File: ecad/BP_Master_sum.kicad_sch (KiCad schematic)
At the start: 14 parts, among them U11 NE5532, U19 NE5532, U20 PGA231x, U3 NE5532

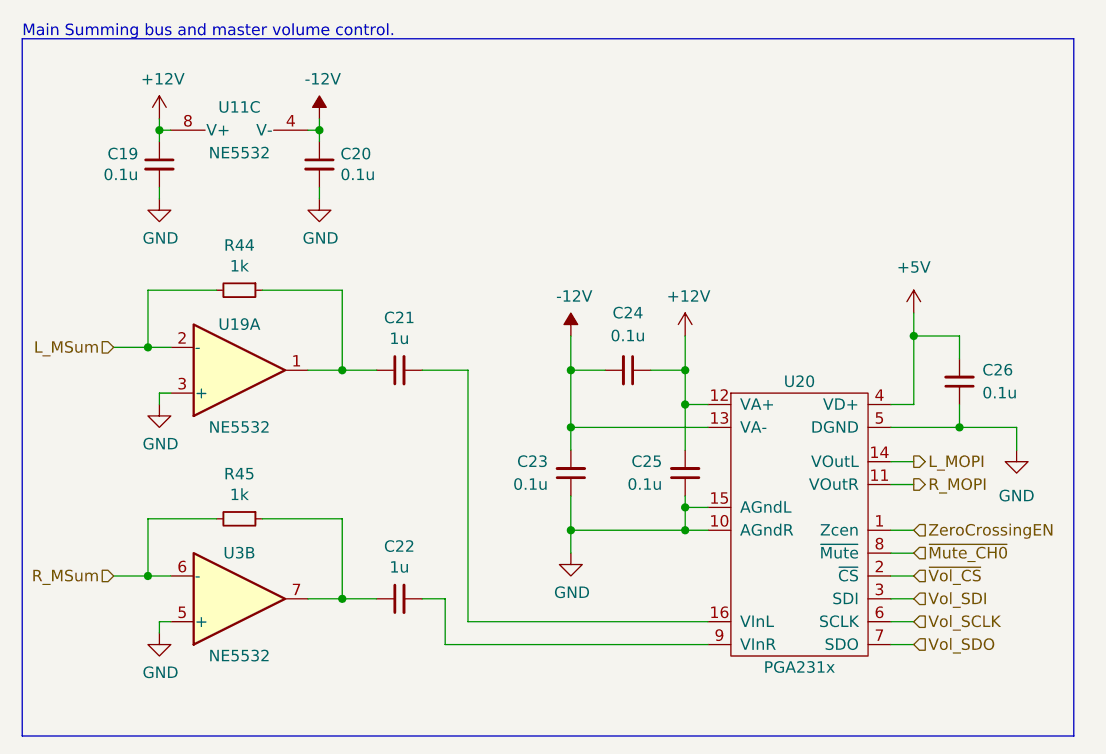
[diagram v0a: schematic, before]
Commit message: Update to Kicad 7 and generate PDF schematic.
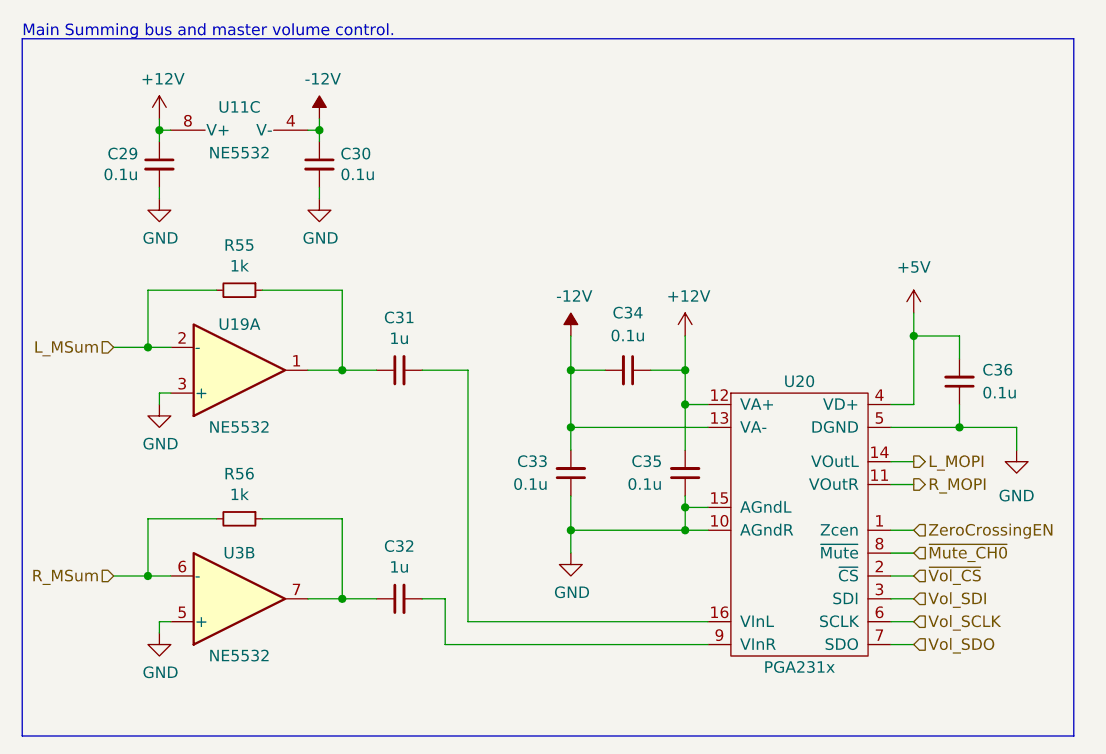
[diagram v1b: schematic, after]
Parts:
- renumbered C19 to C29, C20 to C30, C21 to C31, C22 to C32, C23 to C33, C24 to C34, C25 to C35, C26 to C36, R44 to R55, R45 to R56

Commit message: Fixes to footprint numbering in multi-unit parts.
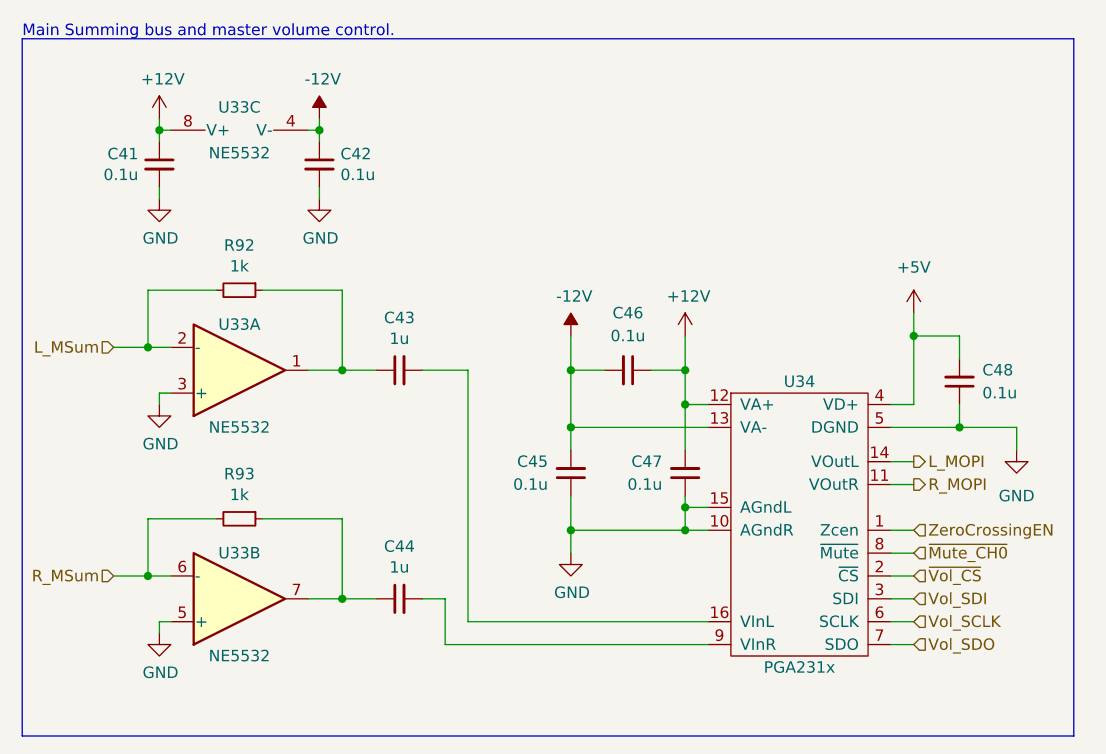
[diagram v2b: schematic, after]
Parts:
- renumbered C29 to C41, C30 to C42, C31 to C43, C32 to C44, C33 to C45, C34 to C46, C35 to C47, C36 to C48, R55 to R92, R56 to R93, U11 to U33, U19 to U33, U3 to U33, U20 to U34
